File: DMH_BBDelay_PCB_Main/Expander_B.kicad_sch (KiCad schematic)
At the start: 23 parts, among them U27 SSI2162, U28 TL074

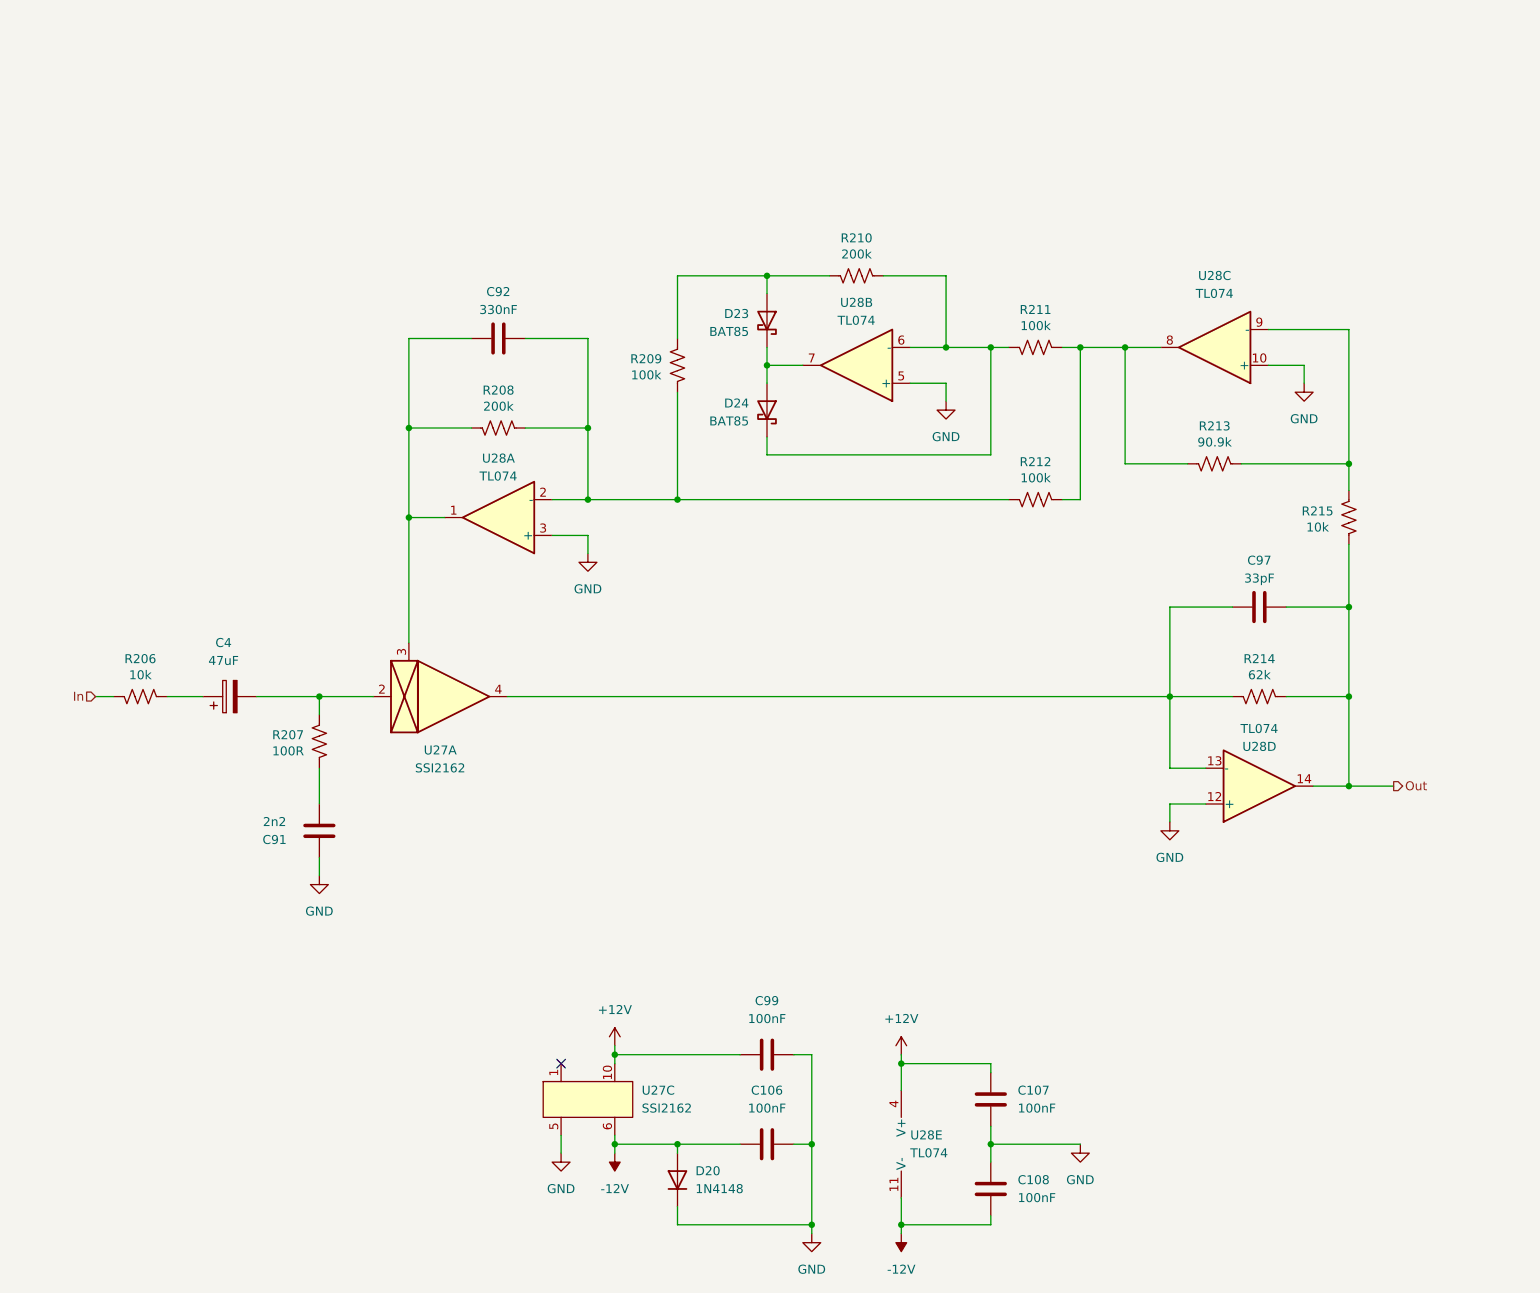
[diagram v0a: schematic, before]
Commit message: Designed Expander circuits
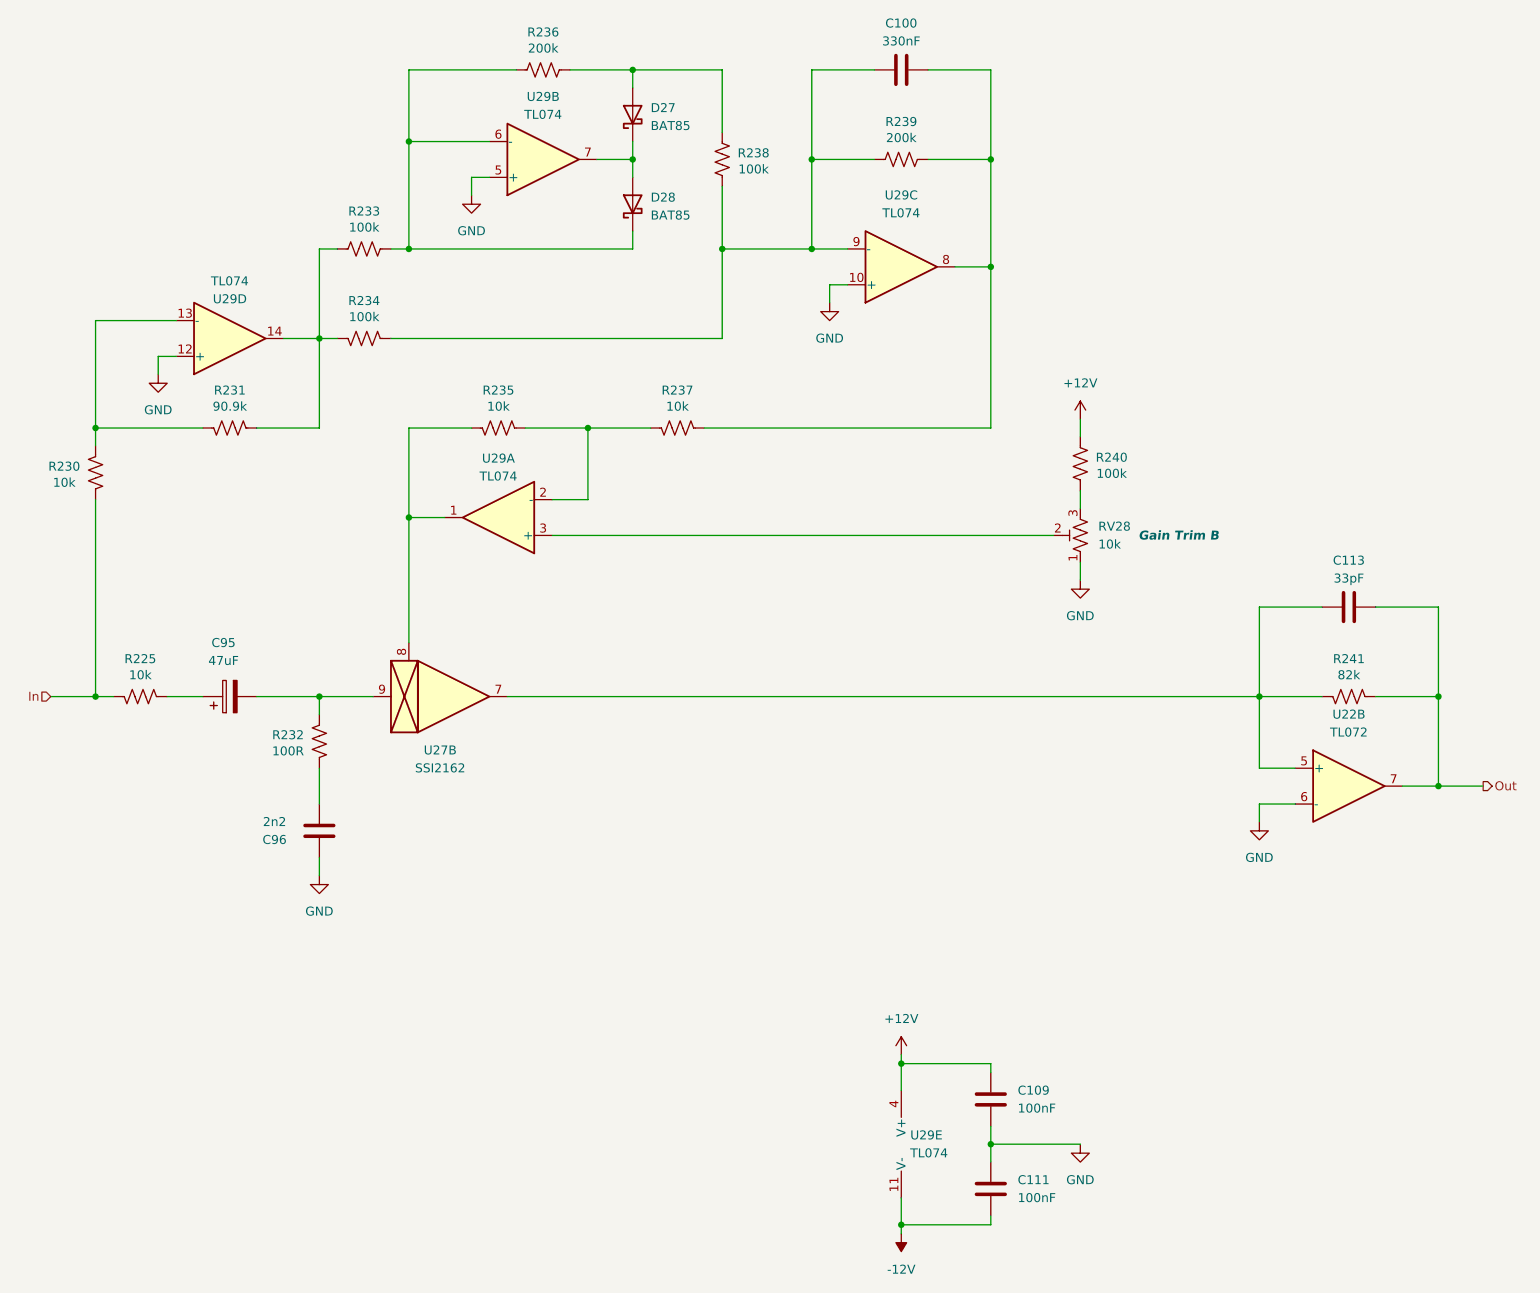
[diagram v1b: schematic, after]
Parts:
- removed C106, C107, C108, C99: 100nF, Capacitor_THT:C_Disc_D4.3mm_W1.9mm_P5.00mm, symbol Device:C
- removed D20: 1N4148, Diode_THT:D_DO-35_SOD27_P7.62mm_Horizontal, symbol Diode:1N4148
- removed R213: 90.9k, Resistor_THT:R_Axial_DIN0207_L6.3mm_D2.5mm_P7.62mm_Horizontal, symbol Device:R_US
- removed R215: 10k, Resistor_THT:R_Axial_DIN0207_L6.3mm_D2.5mm_P7.62mm_Horizontal, symbol Device:R_US
- removed U27: SSI2162, Package_SO:SSOP-10_3.9x4.9mm_P1.00mm, symbol SynthStuff:SSI2162
- removed unit 4 of U28
- added C109, C111: 100nF, Capacitor_THT:C_Disc_D4.3mm_W1.9mm_P5.00mm, symbol Device:C
- added R230, R237: 10k, Resistor_THT:R_Axial_DIN0207_L6.3mm_D2.5mm_P7.62mm_Horizontal, symbol Device:R_US
- added R231: 90.9k, Resistor_THT:R_Axial_DIN0207_L6.3mm_D2.5mm_P7.62mm_Horizontal, symbol Device:R_US
- added R239: 200k, Resistor_THT:R_Axial_DIN0207_L6.3mm_D2.5mm_P7.62mm_Horizontal, symbol Device:R_US
- added R240: 100k, Resistor_THT:R_Axial_DIN0207_L6.3mm_D2.5mm_P7.62mm_Horizontal, symbol Device:R_US
- added RV28: 10k, Potentiometer_THT:Potentiometer_Bourns_3296X_Horizontal, symbol Device:R_Potentiometer_Trim_US
- added U22: TL072, Package_DIP:DIP-8_W7.62mm_Socket, symbol Amplifier_Operational:TL072
- added U27: SSI2162, Package_SO:SSOP-10_3.9x4.9mm_P1.00mm, symbol SynthStuff:SSI2162
- added unit 4 of U29
- R235: renamed from R208; value 200k -> 10k
- R241: renamed from R214; value 62k -> 82k
- renumbered C92 to C100, C97 to C113, C4 to C95, C91 to C96, D23 to D27, D24 to D28, R206 to R225, R207 to R232, R211 to R233, R212 to R234, R210 to R236, R209 to R238, U28 to U29
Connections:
- net +12V: now also C109.1, R240.2
- net -12V: now also C111.2
- net GND: now also C109.2, C111.1, RV28.1, U22.6 (-), U29.12 (+); no longer U29.3 (+)
- net In: now also R230.1
- net Out: now also U22.7
- net at U29.9 (-): now also C100.1, R234.2, R238.1, R239.2
- net at R235.1, U29.1: now also U27.8 (Vc_2); no longer C100.1
- net at C113.1, R241.1: now also U22.5 (+), U27.7 (Out_2)
- net at C95.2, R232.2: now also U27.9 (In_2)
- new net: C100.2, R237.2, R239.1, U29.8
- new net: R235.2, R237.1, U29.2 (-)
- new net: RV28.2, U29.3 (+)
- new net: R230.2, R231.1, U29.13 (-)
- new net: R231.2, R233.2, R234.1, U29.14
- new net: R240.1, RV28.3
- no-connect marks 1 -> 0
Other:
- moved on the sheet: C100, C113, D27, D28, R233, R234, R236, R238, R241, U29B, U29C

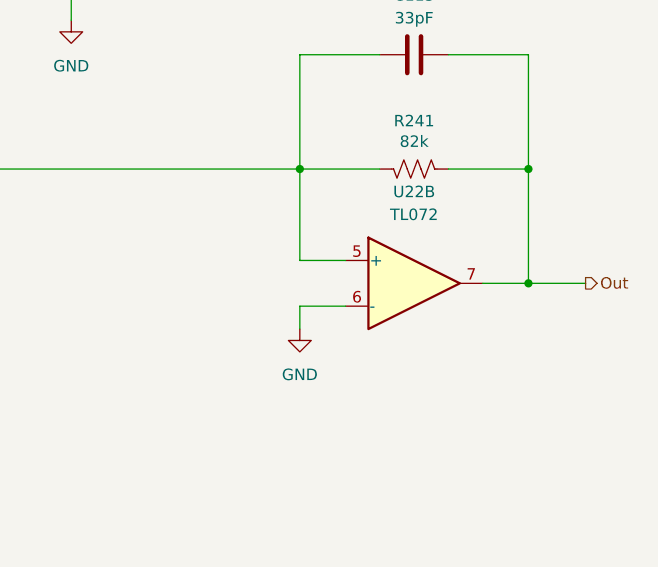
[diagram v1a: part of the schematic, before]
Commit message: Fixed mistake with expander output opamp
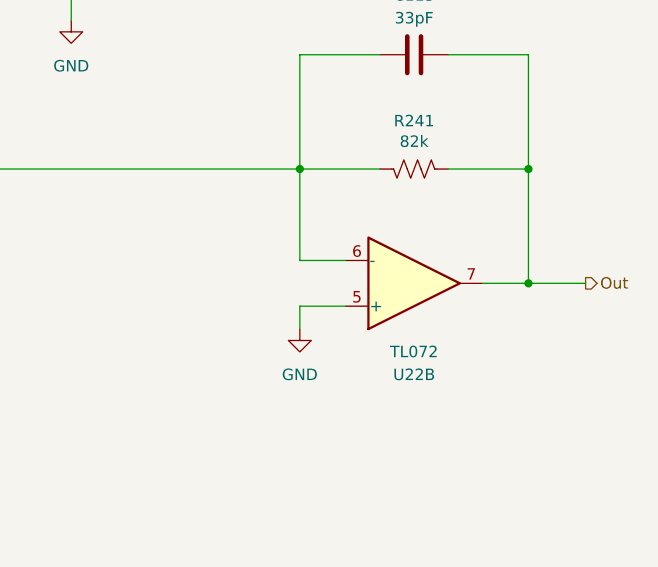
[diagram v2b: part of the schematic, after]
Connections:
- net GND: now also U22.5 (+); no longer U22.6 (-)
- net at C113.1, R241.1, U27.7 (Out_2): now also U22.6 (-); no longer U22.5 (+)
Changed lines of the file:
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@@
 		(lib_id "Amplifier_Operational:TL072")
 		(at 203.2 127 0)
+		(mirror x)
 		(unit 2)
 		(body_style 1)
@@
 		(in_pos_files yes)
 		(dnp no)
-		(fields_autoplaced yes)
 		(property "Reference" "U22"
-			(at 203.2 116.84 0)
+			(at 203.2 137.16 0)
 			(show_name no)
 			(do_not_autoplace no)
@@
 		)
 		(property "Value" "TL072"
-			(at 203.2 119.38 0)
+			(at 203.2 134.62 0)
 			(show_name no)
 			(do_not_autoplace no)

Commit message: Tweaked compander
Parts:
- C96: now not fitted
- R232: value 100R -> 1k
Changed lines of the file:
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@@
 			)
 		)
-		(property "Value" "100R"
+		(property "Value" "1k"
 			(at 52.705 122.047 0)
 			(show_name no)
@@
 		(on_board yes)
 		(in_pos_files yes)
-		(dnp no)
+		(dnp yes)
 		(property "Reference" "C96"
 			(at 50.8 134.62 0)

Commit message: Scaled up components in Tone Control part
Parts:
- R239: value 200k -> 100k
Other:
- note added: "Changed resistor from 100R to 1k, and replaced 2n2 with short"
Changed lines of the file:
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@@
 		(comment 1 "PCB for 10cm Kosmo format synthesizer module")
 	)
+	(circle
+		(center 54.864 120.142)
+		(radius 5.08)
+		(stroke
+			(width 0)
+			(type default)
+		)
+		(fill
+			(type none)
+		)
+	)
+	(text "Changed resistor from 100R to 1k,\nand replaced 2n2 with short"
+		(exclude_from_sim no)
+		(at 34.29 128.27 0)
+		(effects
+			(font
+				(size 1.27 1.27)
+			)
+		)
+	)
 	(junction
 		(at 127 38.1)
@@
 			)
 		)
-		(property "Value" "200k"
+		(property "Value" "100k"
 			(at 139.7 35.052 90)
 			(show_name no)
